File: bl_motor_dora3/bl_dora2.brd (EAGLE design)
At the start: 85 x 50.8 mm, 91 parts

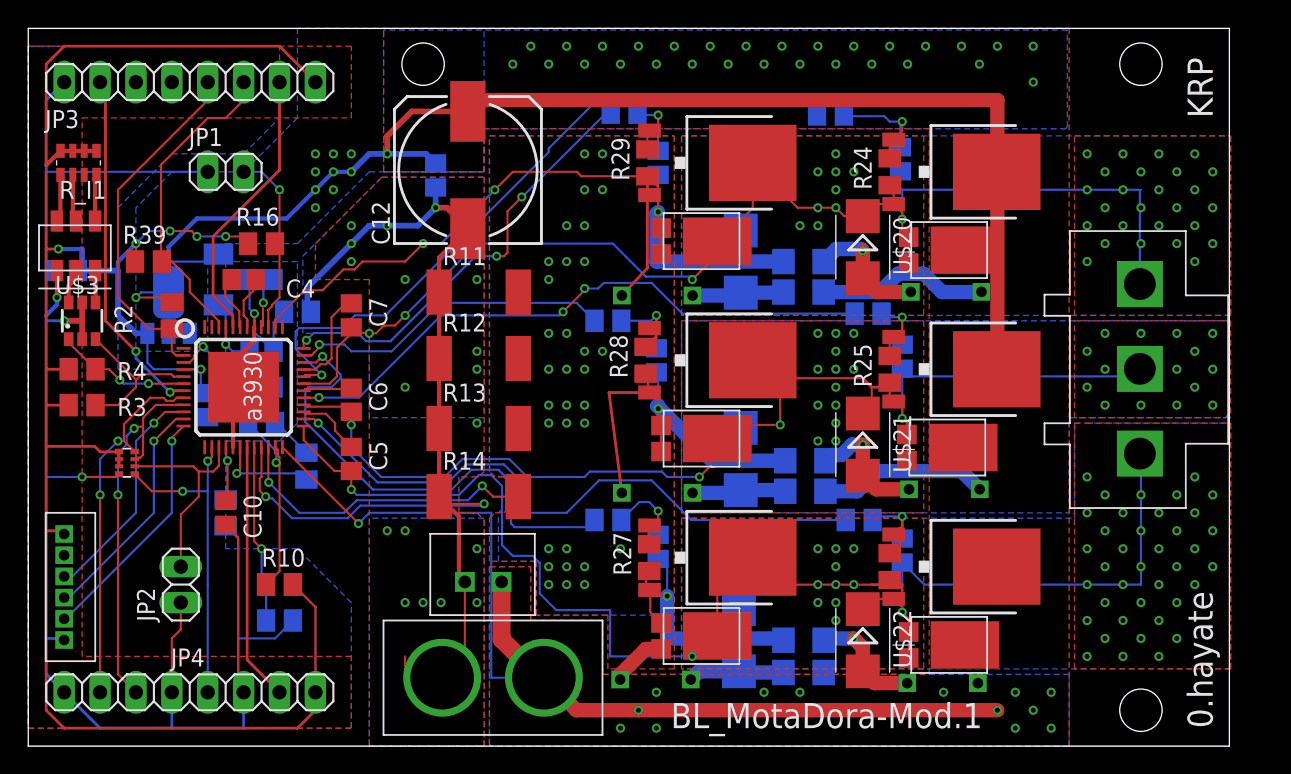
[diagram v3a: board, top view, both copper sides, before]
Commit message: 完成品
配線の修正などをおこなった
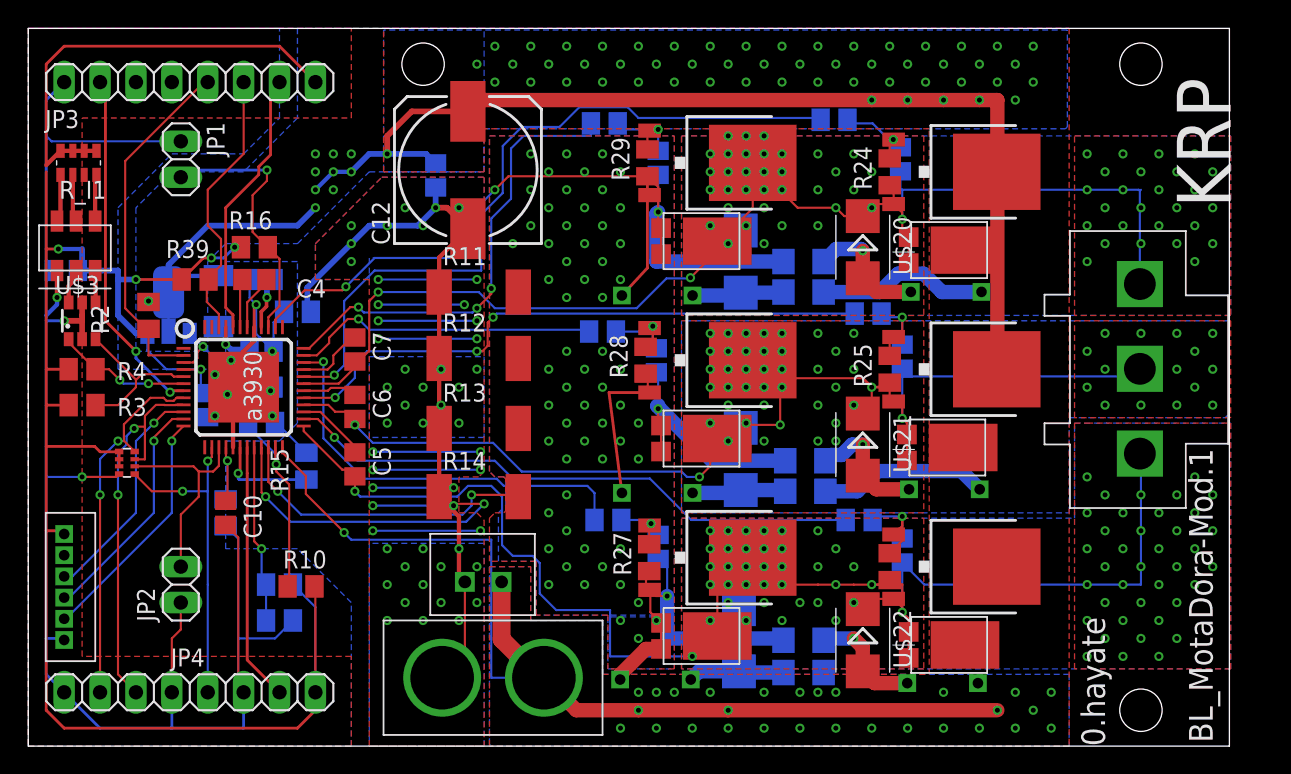
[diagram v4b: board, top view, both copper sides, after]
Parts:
- moved R39 3.54 mm to (11.8, 33.0)
- moved JP1 3.30 mm to (10.8, 41.5), turned to 270 degrees
- moved C7 2.43 mm to (23.1, 28.1)
- moved R2 1.65 mm to (8.51, 30.5)
- moved R23 1.59 mm to (40.8, 44.1)
- moved R10 1.53 mm to (19.3, 11.3)
- moved U$6 1.52 mm to (13.5, 31.5)
- moved R22 0.85 mm to (40.6, 29.3)
- moved C4 0.76 mm to (16.0, 33.0)
- moved R16 0.57 mm to (16.0, 35.3)
- moved C6 0.57 mm to (23.1, 24.0)
- moved R18 0.46 mm to (57.0, 44.3)
- moved C5 0.46 mm to (23.1, 19.9)
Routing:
- net GND: track 79.2 -> 137.1 mm, vias 20 -> 53
- net N$33: track 35.3 -> 29.5 mm
- net ESF: track 13.4 -> 19.0 mm
- net VCC: track 199.6 -> 195.1 mm, vias 54 -> 93
- net N$37: track 45.5 -> 41.4 mm
- net V5: track 153.1 -> 149.0 mm, vias 6 -> 5
- net N$25: track 9.18 -> 6.05 mm
- net N$28: track 8.05 -> 4.93 mm
- net COAST: track 22.6 -> 19.6 mm
- net N$50: track 87.6 -> 85.0 mm, vias 32 -> 57
- net N$29: track 8.60 -> 6.39 mm
- net N$35: track 49.6 -> 51.8 mm
- net N$18: track 7.02 -> 4.91 mm
- net N$31: track 31.1 -> 33.0 mm
- net N$23: track 6.12 -> 4.60 mm
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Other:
- board text added: "A"
- board text added: "B"
- board text added: "C"

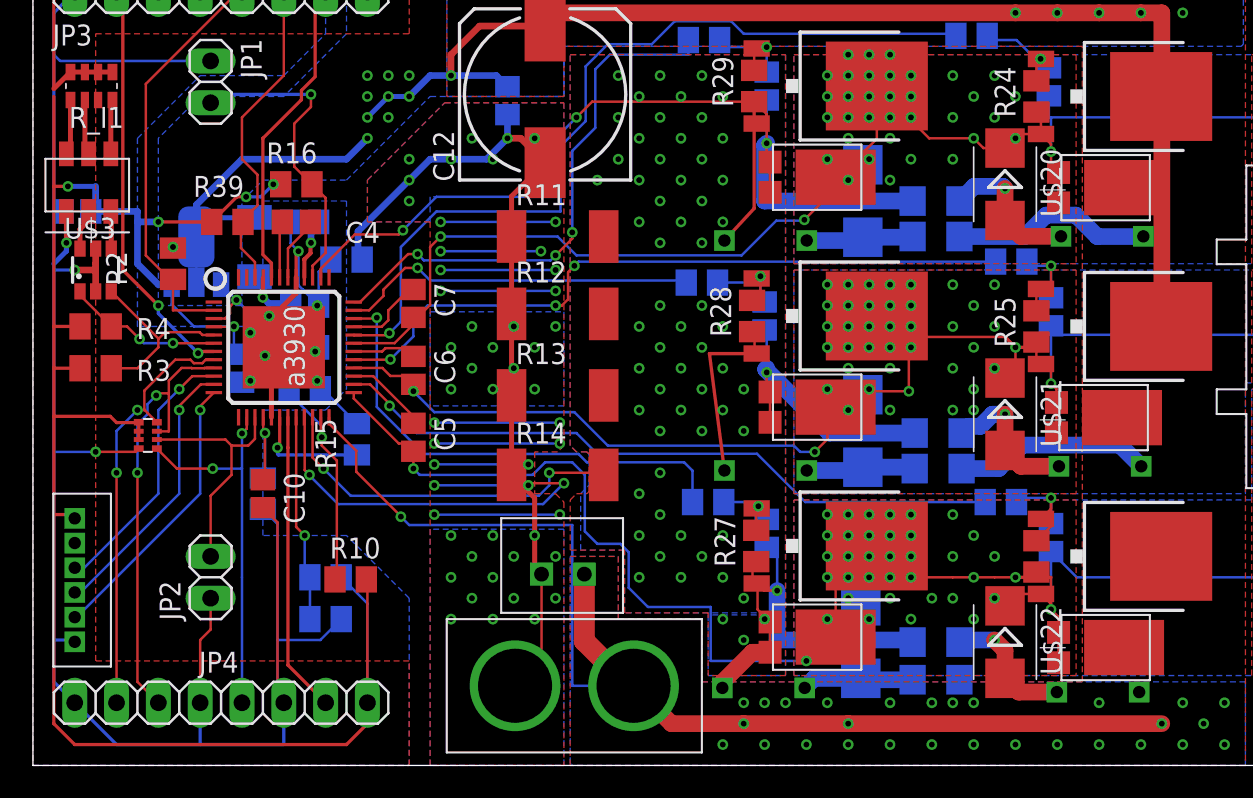
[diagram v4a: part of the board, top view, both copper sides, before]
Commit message: スケマチックの抵抗の値がおかしかった
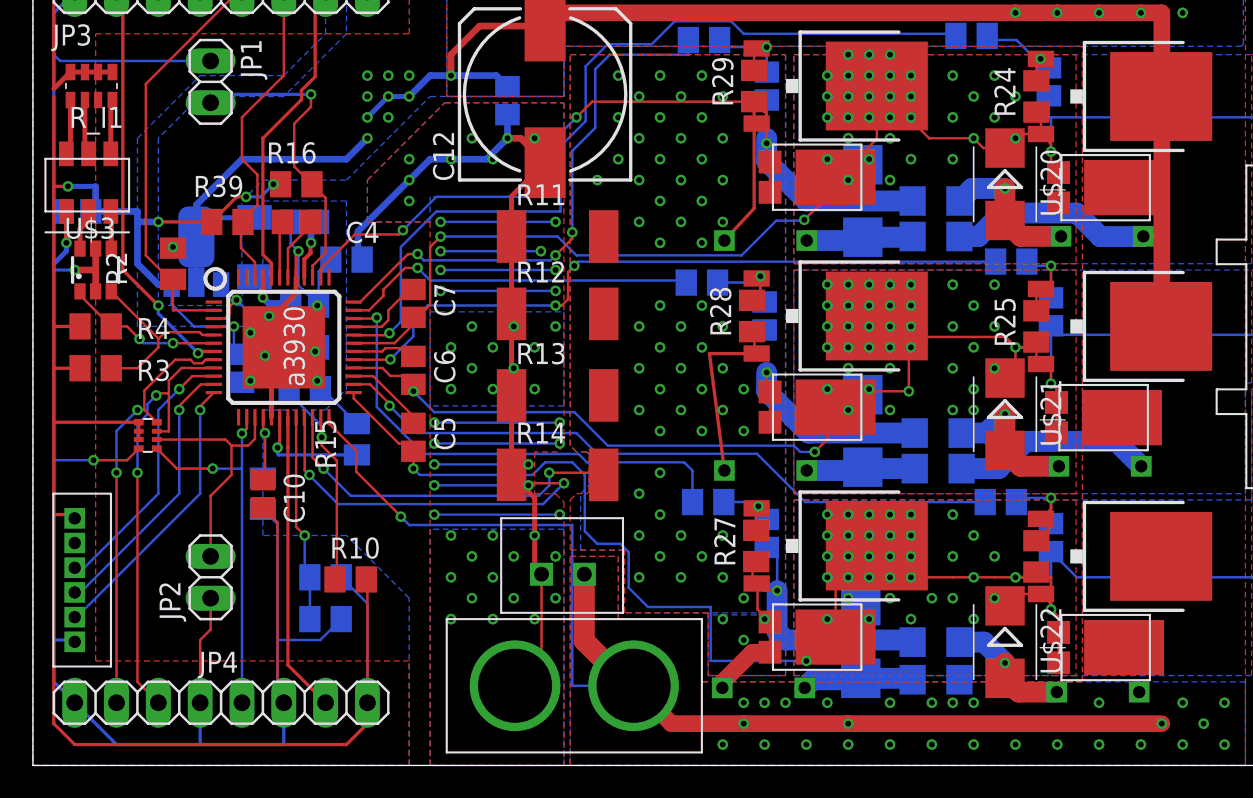
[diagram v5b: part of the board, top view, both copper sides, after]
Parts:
- R26, R30, R31, R32, R6, R7: value 47 -> 22
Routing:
- net N$40: track 140.0 -> 136.2 mm
- net N$41: track 8.27 -> 7.72 mm

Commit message: エンハンスドver
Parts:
- R10: value 47k -> 20k
- R5: value 22k -> 39k
- R8: value 39k -> 22k
- R9: value 10k -> 3.3k
- U$23: value ZH_6P -> ZH_6P_L; device user:ZH_6P -> user:ZH_6P_L
- moved R39 4.57 mm to (11.9, 37.6)
- moved U$23 2.19 mm to (4.70, 16.9), flipped to the bottom
- moved R2 1.63 mm to (7.49, 29.2), turned to 0 degrees
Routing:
- net V5: track 148.9 -> 156.6 mm
- net VCC: track 195.4 -> 191.7 mm, vias 93 -> 112
- net AGND: track 158.1 -> 160.3 mm
- net BRAKE: track 26.1 -> 27.2 mm
- net H1: track 16.2 -> 15.4 mm
- net H2: track 16.8 -> 16.0 mm

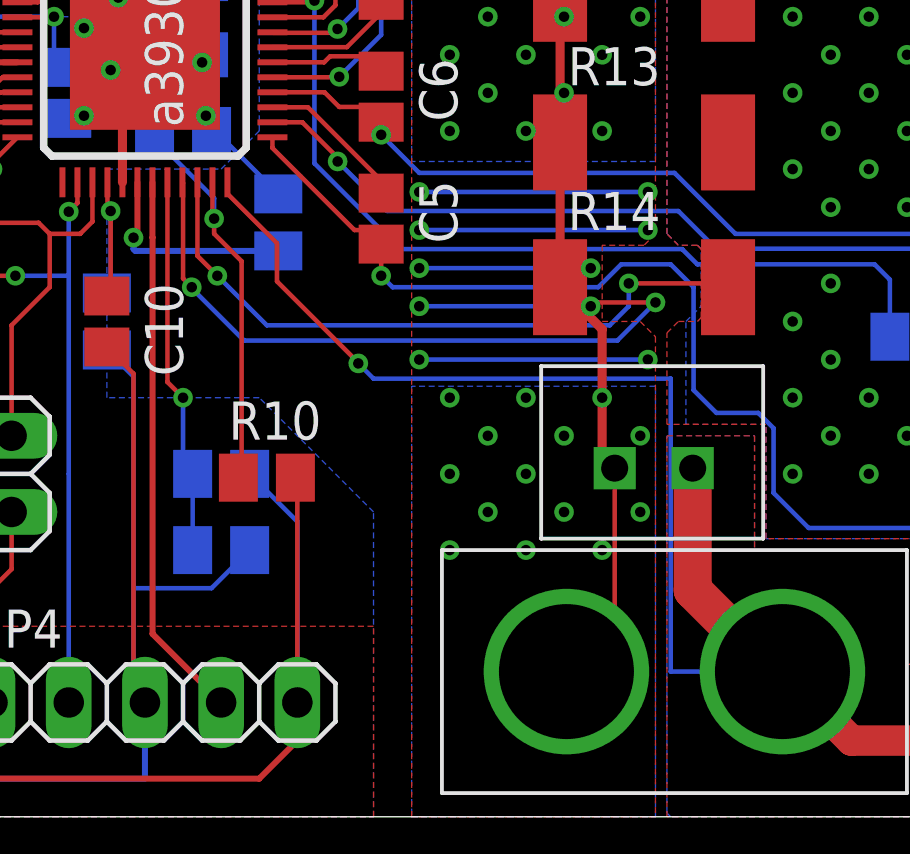
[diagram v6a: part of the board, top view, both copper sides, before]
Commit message: シャント抵抗ラインにローパスフィルタの追加
電流制限、電流測定がつかいもんにならんかったからノイズを消すためにローパスフィルタをシャント抵抗の電位差を測るラインに追加
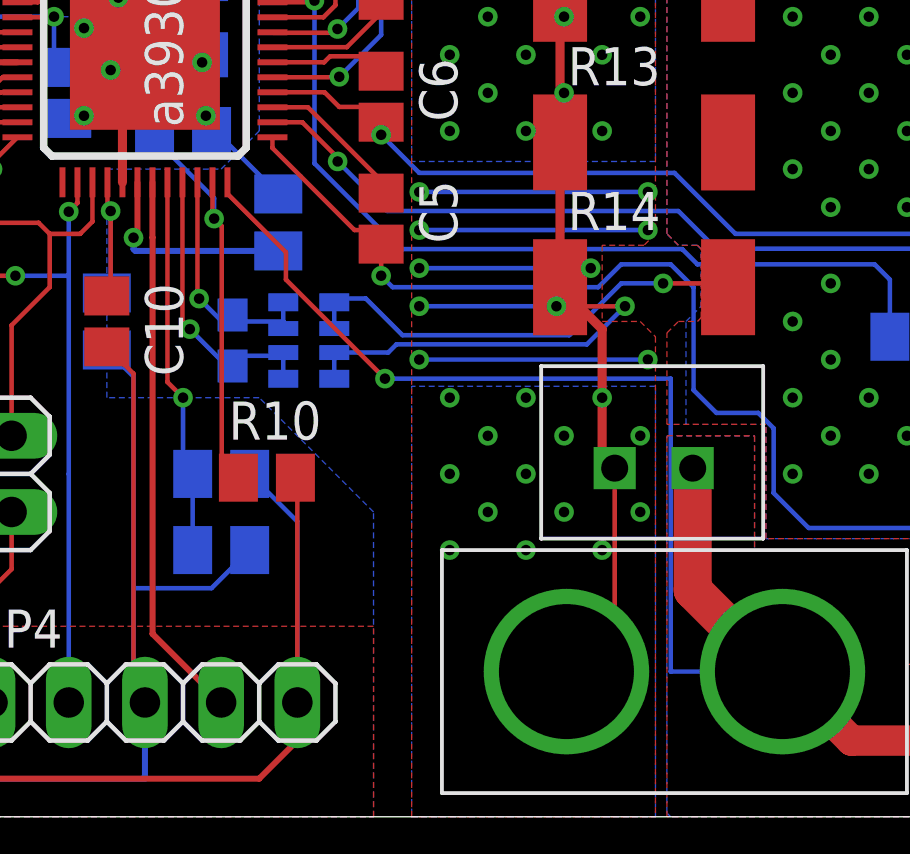
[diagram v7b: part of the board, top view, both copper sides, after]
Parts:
- added C19: 2.2n, rcl:C1608
- added R_I2: 1k, user_rcl:0603X4RESISTOR
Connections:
- removed net N$40: C14.2, C15.2, C16.2, F_C1.P$2, F_C2.P$2, F_C6.P$2, R11.2, R12.2, R13.2, R14.2, R27.1, R28.1, R29.1, R30.1, R31.1, R32.1, U$1.PIN22, U$1.PIN38, U$10.PIN3_S, U$12.PIN3_S, U$14.A1, U$14.A2, U$15.A1, U$15.A2, U$18.A1, U$18.A2, U$8.PIN3_S
- new net N$20: C19.1, R_I2.7, R_I2.8, U$1.PIN22
- new net N$6: C14.2, C15.2, C16.2, F_C1.P$2, F_C2.P$2, F_C6.P$2, R11.2, R12.2, R13.2, R14.2, R27.1, R28.1, R29.1, R30.1, R31.1, R32.1, R_I2.1, R_I2.2, U$1.PIN38, U$10.PIN3_S, U$12.PIN3_S, U$14.A1, U$14.A2, U$15.A1, U$15.A2, U$18.A1, U$18.A2, U$8.PIN3_S
- new net N$9: C19.2, R_I2.5, R_I2.6, U$1.PIN21
- net GND: now also R_I2.3, R_I2.4; no longer U$1.PIN21
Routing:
- net N$40: track 136.2 -> 0.00 mm, vias 67 -> 0
- net N$6: track 0.00 -> 129.4 mm, vias 0 -> 66
- net GND: track 137.1 -> 124.9 mm, vias 53 -> 52
- net N$9: track 0.00 -> 9.64 mm, vias 0 -> 1
- net N$20: track 0.00 -> 8.14 mm, vias 0 -> 1
- added copper zone on layer 1, net N$6
- added copper zone on layer 16, net N$6
- removed copper zone on layer 1, net N$40
- removed copper zone on layer 16, net N$40
